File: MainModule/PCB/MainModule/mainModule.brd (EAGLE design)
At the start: 160 x 100 mm, 13 parts, among them U1 LM5007MM

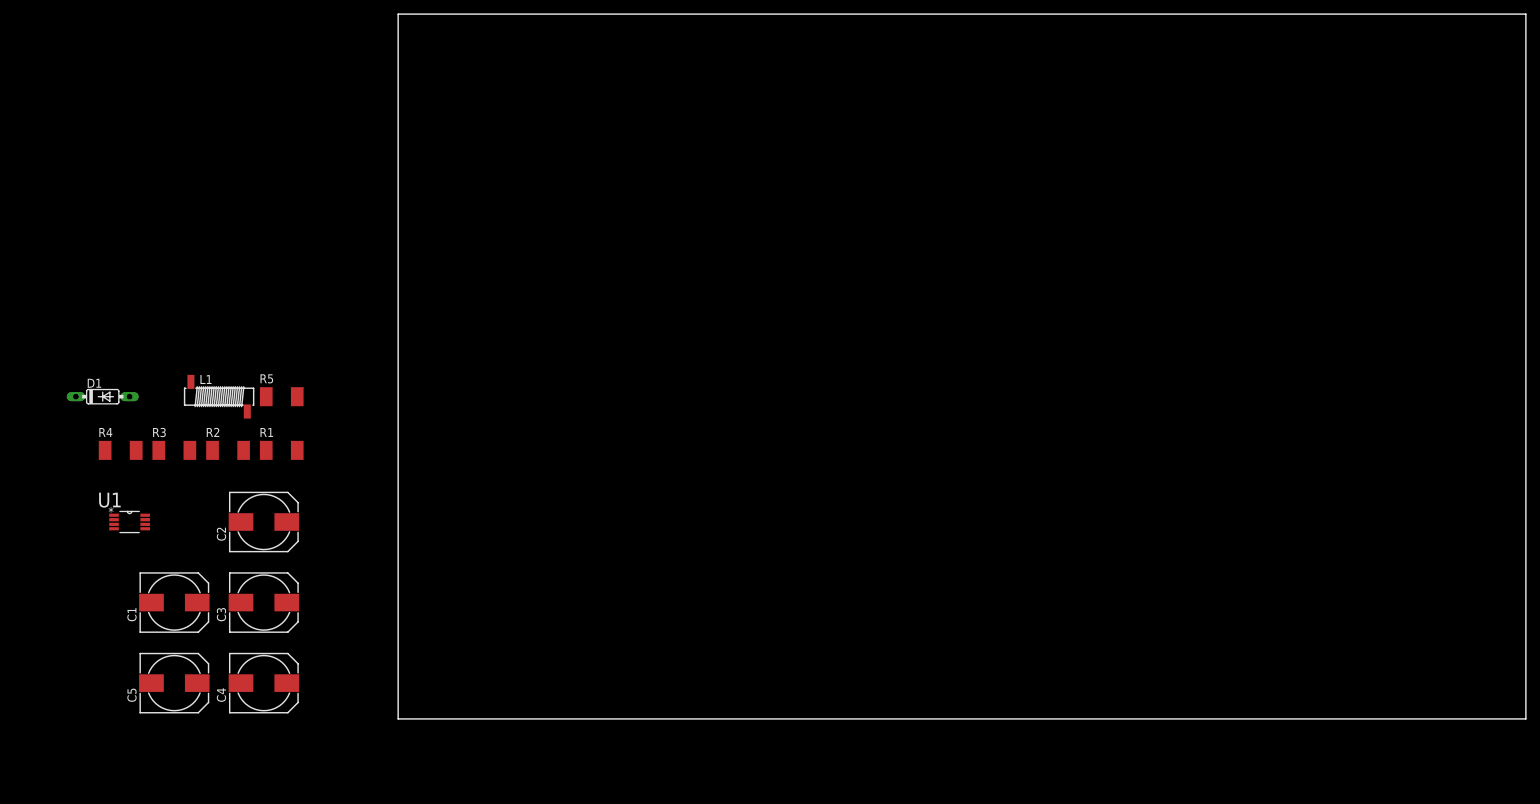
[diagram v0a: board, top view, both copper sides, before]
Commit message: Changed capacitor packages in to power supply schematic (switching)
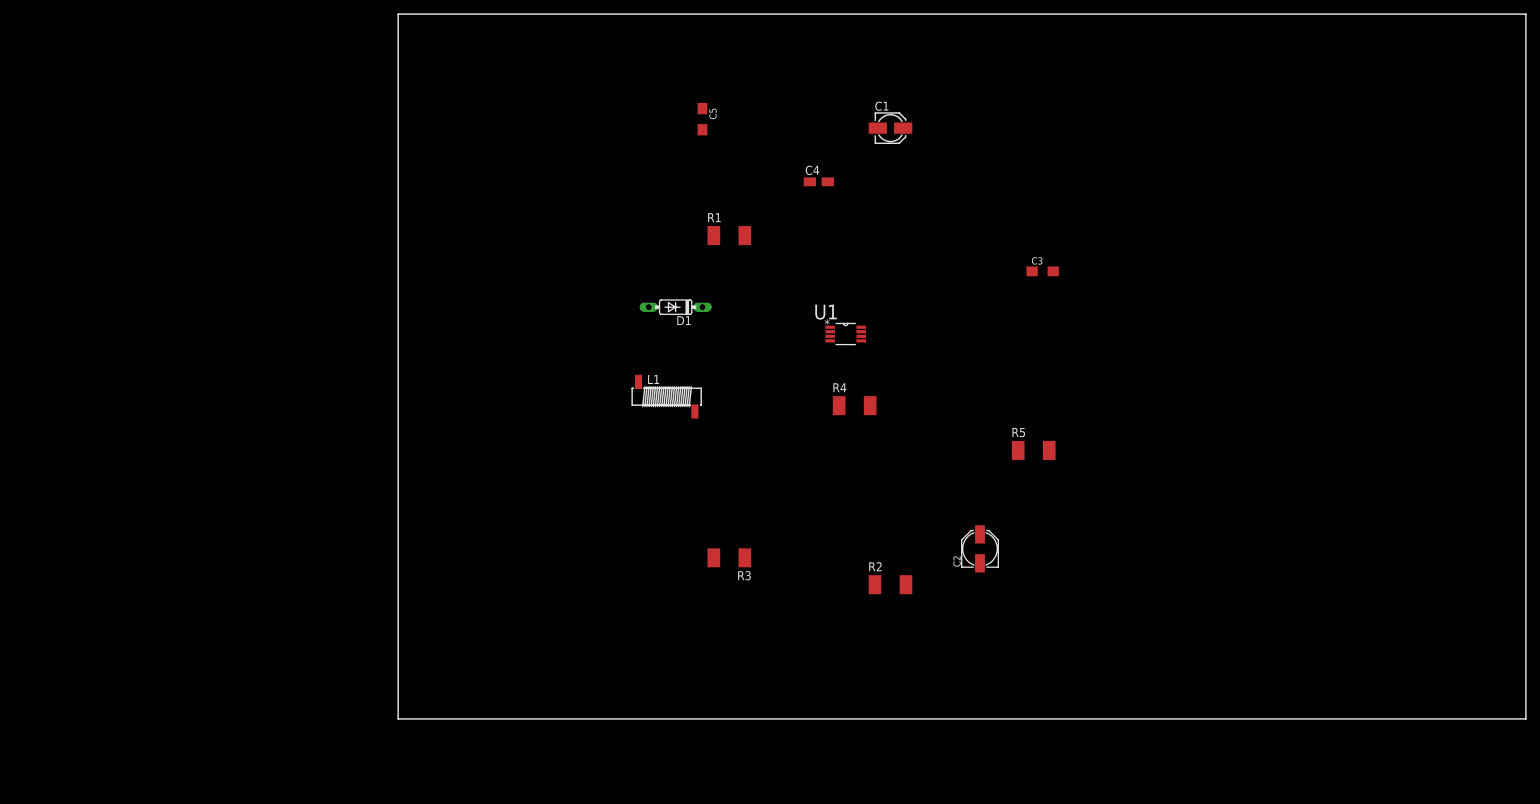
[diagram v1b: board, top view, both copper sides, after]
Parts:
- C1: device resistor:140CLH-0810 -> resistor:153CLV-0405
- C2: device resistor:140CLH-0810 -> resistor:PANASONIC_C
- C3: value 0.1uF, 50V -> 100nF, 50V; device resistor:140CLH-0810 -> resistor:SMC_A
- C4: value 0.01uF, 50V -> 10nF, 50V; device resistor:140CLH-0810 -> resistor:R/2012-12W
- C5: value 0.1uF, 100V -> 100nF, 100V; device resistor:140CLH-0810 -> resistor:SMC_A
- moved C1 121.9 mm to (69.8, 83.8)
- moved C3 120.1 mm to (91.4, 63.5)
- moved C5 109.6 mm to (43.2, 85.1), turned to 270 degrees
- moved R5 107.0 mm to (90.2, 38.1)
- moved C4 106.1 mm to (59.7, 76.2)
- moved U1 105.0 mm to (63.5, 54.6)
- moved R4 104.3 mm to (64.8, 44.5)
- moved C2 101.7 mm to (82.5, 24.1), turned to 90 degrees
- moved R2 95.9 mm to (69.8, 19.1)
- moved D1 82.3 mm to (39.4, 58.4), turned to 180 degrees
- moved R3 80.2 mm to (47.0, 22.9), turned to 180 degrees
- moved R1 70.4 mm to (47.0, 68.6)
- moved L1 63.5 mm to (38.1, 45.7)
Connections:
- net GND: no longer C1.-, C2.-, C3.-, C5.-
- net N$5: no longer C4.+
- net N$6: no longer C4.-
- net N$7: no longer C3.+
- net N$9: no longer C2.+
- net VIN(12-75V): no longer C1.+, C5.+
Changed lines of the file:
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@@
 </autorouter>
 <elements>
-<element name="U1" library="LM5007" package="SOP65P490X109-8N" value="LM5007MM" x="-38.1" y="27.94">
-<attribute name="PACKAGE" value="SOP-8" x="0" y="0" size="1.778" layer="27" display="off"/>
-<attribute name="OC_NEWARK" value="97K3542" x="0" y="0" size="1.778" layer="27" display="off"/>
-<attribute name="MPN" value="LM5007MM" x="0" y="0" size="1.778" layer="27" display="off"/>
-<attribute name="SUPPLIER" value="TEXAS INSTRUMENTS" x="0" y="0" size="1.778" layer="27" display="off"/>
-<attribute name="OC_FARNELL" value="9779345" x="0" y="0" size="1.778" layer="27" display="off"/>
+<element name="U1" library="LM5007" package="SOP65P490X109-8N" value="LM5007MM" x="63.5" y="54.61">
+<attribute name="PACKAGE" value="SOP-8" x="101.6" y="26.67" size="1.778" layer="27" display="off"/>
+<attribute name="OC_NEWARK" value="97K3542" x="101.6" y="26.67" size="1.778" layer="27" display="off"/>
+<attribute name="MPN" value="LM5007MM" x="101.6" y="26.67" size="1.778" layer="27" display="off"/>
+<attribute name="SUPPLIER" value="TEXAS INSTRUMENTS" x="101.6" y="26.67" size="1.778" layer="27" display="off"/>
+<attribute name="OC_FARNELL" value="9779345" x="101.6" y="26.67" size="1.778" layer="27" display="off"/>
 </element>
-<element name="C1" library="resistor" package="140CLH-0810" value="1uF, 100V" x="-31.75" y="16.51"/>
-<element name="C2" library="resistor" package="140CLH-0810" value="15uF, 25V" x="-19.05" y="27.94"/>
-<element name="C3" library="resistor" package="140CLH-0810" value="0.1uF, 50V" x="-19.05" y="16.51"/>
-<element name="C4" library="resistor" package="140CLH-0810" value="0.01uF, 50V" x="-19.05" y="5.08"/>
-<element name="C5" library="resistor" package="140CLH-0810" value="0.1uF, 100V" x="-31.75" y="5.08"/>
-<element name="L1" library="inductor-neosid" package="SM-Z15" value="100uH" x="-25.4" y="45.72">
-<attribute name="OC_NEWARK" value="unknown" x="0" y="0" size="1.778" layer="27" display="off"/>
-<attribute name="MPN" value="" x="0" y="0" size="1.778" layer="27" display="off"/>
-<attribute name="MF" value="" x="0" y="0" size="1.778" layer="27" display="off"/>
-<attribute name="OC_FARNELL" value="unknown" x="0" y="0" size="1.778" layer="27" display="off"/>
+<element name="C1" library="resistor" package="153CLV-0405" value="1uF, 100V" x="69.85" y="83.82"/>
+<element name="C2" library="resistor" package="PANASONIC_C" value="15uF, 25V" x="82.55" y="24.13" rot="R90"/>
+<element name="C3" library="resistor" package="SMC_A" value="100nF, 50V" x="91.44" y="63.5"/>
+<element name="C4" library="resistor" package="R/2012-12W" value="10nF, 50V" x="59.69" y="76.2"/>
+<element name="C5" library="resistor" package="SMC_A" value="100nF, 100V" x="43.18" y="85.09" rot="R270"/>
+<element name="L1" library="inductor-neosid" package="SM-Z15" value="100uH" x="38.1" y="45.72">
+<attribute name="OC_NEWARK" value="unknown" x="63.5" y="0" size="1.778" layer="27" display="off"/>
+<attribute name="MPN" value="" x="63.5" y="0" size="1.778" layer="27" display="off"/>
+<attribute name="MF" value="" x="63.5" y="0" size="1.778" layer="27" display="off"/>
+<attribute name="OC_FARNELL" value="unknown" x="63.5" y="0" size="1.778" layer="27" display="off"/>
 </element>
-<element name="R1" library="rcl" package="R2010" value="200K" x="-16.51" y="38.1"/>
-<element name="R2" library="rcl" package="R2010" value="100K" x="-24.13" y="38.1"/>
-<element name="R3" library="rcl" package="R2010" value="1K" x="-31.75" y="38.1"/>
-<element name="R4" library="rcl" package="R2010" value="1K" x="-39.37" y="38.1"/>
-<element name="R5" library="rcl" package="R2010" value="1ohm" x="-16.51" y="45.72"/>
-<element name="D1" library="diode" package="DO35-7" value="1N4148DO35-7" x="-41.91" y="45.72"/>
+<element name="R1" library="rcl" package="R2010" value="200K" x="46.99" y="68.58"/>
+<element name="R2" library="rcl" package="R2010" value="100K" x="69.85" y="19.05"/>
+<element name="R3" library="rcl" package="R2010" value="1K" x="46.99" y="22.86" rot="R180"/>
+<element name="R4" library="rcl" package="R2010" value="1K" x="64.77" y="44.45"/>
+<element name="R5" library="rcl" package="R2010" value="1ohm" x="90.17" y="38.1"/>
+<element name="D1" library="diode" package="DO35-7" value="1N4148DO35-7" x="39.37" y="58.42" rot="R180"/>
 </elements>
 <signals>
@@
 <contactref element="U1" pad="3"/>
 <contactref element="R2" pad="2"/>
-<wire x1="-40.3098" y1="27.6098" x2="-21.93" y2="38.1" width="0" layer="19" extent="1-1"/>
+<wire x1="61.2902" y1="54.2798" x2="72.05" y2="19.05" width="0" layer="19" extent="1-1"/>
 </signal>
 <signal name="N$3">
 <contactref element="U1" pad="6"/>
 <contactref element="R1" pad="1"/>
-<wire x1="-35.8902" y1="27.6098" x2="-18.71" y2="38.1" width="0" layer="19" extent="1-1"/>
+<wire x1="65.7098" y1="54.2798" x2="44.79" y2="68.58" width="0" layer="19" extent="1-1"/>
 </signal>
 <signal name="VIN(12-75V)">
 <contactref element="U1" pad="8"/>
 <contactref element="R1" pad="2"/>
-<contactref element="C1" pad="+"/>
-<contactref element="C5" pad="+"/>
-<wire x1="-35.8902" y1="28.9052" x2="-14.31" y2="38.1" width="0" layer="19" extent="1-1"/>
-<wire x1="-28.5" y1="16.51" x2="-35.8902" y2="28.9052" width="0" layer="19" extent="1-1"/>
-<wire x1="-28.5" y1="5.08" x2="-28.5" y2="16.51" width="0" layer="19" extent="1-1"/>
+<wire x1="65.7098" y1="55.5752" x2="49.19" y2="68.58" width="0" layer="19" extent="1-1"/>
+<wire x1="73.1" y1="83.82" x2="65.7098" y2="55.5752" width="0" layer="19" extent="1-1"/>
+<wire x1="43.18" y1="81.84" x2="73.1" y2="83.82" width="0" layer="19" extent="1-1"/>
 </signal>
 <signal name="N$5">
-<contactref element="C4" pad="+"/>
 <contactref element="U1" pad="2"/>
-<wire x1="-40.3098" y1="28.2702" x2="-15.8" y2="5.08" width="0" layer="19" extent="1-1"/>
+<wire x1="61.2902" y1="54.9402" x2="62.94" y2="76.2" width="0" layer="19" extent="1-1"/>
 </signal>
 <signal name="N$6">
-<contactref element="C4" pad="-"/>
 <contactref element="U1" pad="1"/>
 <contactref element="D1" pad="C"/>
 <contactref element="L1" pad="1"/>
-<wire x1="-45.72" y1="45.72" x2="-29.4" y2="47.82" width="0" layer="19" extent="1-1"/>
-<wire x1="-40.3098" y1="28.9052" x2="-45.72" y2="45.72" width="0" layer="19" extent="1-1"/>
-<wire x1="-22.3" y1="5.08" x2="-40.3098" y2="28.9052" width="0" layer="19" extent="1-1"/>
+<wire x1="43.18" y1="58.42" x2="34.1" y2="47.82" width="0" layer="19" extent="1-1"/>
+<wire x1="61.2902" y1="55.5752" x2="43.18" y2="58.42" width="0" layer="19" extent="1-1"/>
+<wire x1="56.44" y1="76.2" x2="61.2902" y2="55.5752" width="0" layer="19" extent="1-1"/>
 </signal>
 <signal name="GND">
-<contactref element="C3" pad="-"/>
-<contactref element="C1" pad="-"/>
-<contactref element="C5" pad="-"/>
 <contactref element="R2" pad="1"/>
 <contactref element="U1" pad="4"/>
 <contactref element="R4" pad="1"/>
-<contactref element="C2" pad="-"/>
 <contactref element="D1" pad="A"/>
-<wire x1="-35" y1="16.51" x2="-35" y2="5.08" width="0" layer="19" extent="1-1"/>
-<wire x1="-40.3098" y1="26.9748" x2="-35" y2="16.51" width="0" layer="19" extent="1-1"/>
-<wire x1="-41.57" y1="38.1" x2="-40.3098" y2="26.9748" width="0" layer="19" extent="1-1"/>
-<wire x1="-38.1" y1="45.72" x2="-41.57" y2="38.1" width="0" layer="19" extent="1-1"/>
-<wire x1="-22.3" y1="16.51" x2="-35" y2="16.51" width="0" layer="19" extent="1-1"/>
-<wire x1="-22.3" y1="27.94" x2="-22.3" y2="16.51" width="0" layer="19" extent="1-1"/>
-<wire x1="-26.33" y1="38.1" x2="-22.3" y2="27.94" width="0" layer="19" extent="1-1"/>
+<wire x1="66.6" y1="83.82" x2="43.18" y2="88.34" width="0" layer="19" extent="1-1"/>
+<wire x1="61.2902" y1="53.6448" x2="66.6" y2="83.82" width="0" layer="19" extent="1-1"/>
+<wire x1="62.57" y1="44.45" x2="61.2902" y2="53.6448" width="0" layer="19" extent="1-1"/>
+<wire x1="35.56" y1="58.42" x2="62.57" y2="44.45" width="0" layer="19" extent="1-1"/>
+<wire x1="88.19" y1="63.5" x2="66.6" y2="83.82" width="0" layer="19" extent="1-1"/>
+<wire x1="82.55" y1="20.88" x2="88.19" y2="63.5" width="0" layer="19" extent="1-1"/>
+<wire x1="67.65" y1="19.05" x2="82.55" y2="20.88" width="0" layer="19" extent="1-1"/>
 </signal>
 <signal name="N$7">
 <contactref element="U1" pad="7"/>
-<contactref element="C3" pad="+"/>
-<wire x1="-15.8" y1="16.51" x2="-35.8902" y2="28.2702" width="0" layer="19" extent="1-1"/>
+<wire x1="94.69" y1="63.5" x2="65.7098" y2="54.9402" width="0" layer="19" extent="1-1"/>
 </signal>
 <signal name="VOUT(5V)">
@@
 <contactref element="R5" pad="2"/>
 <contactref element="R3" pad="2"/>
-<wire x1="-21.4" y1="43.62" x2="-14.31" y2="45.72" width="0" layer="19" extent="1-1"/>
-<wire x1="-29.55" y1="38.1" x2="-21.4" y2="43.62" width="0" layer="19" extent="1-1"/>
+<wire x1="42.1" y1="43.62" x2="92.37" y2="38.1" width="0" layer="19" extent="1-1"/>
+<wire x1="44.79" y1="22.86" x2="42.1" y2="43.62" width="0" layer="19" extent="1-1"/>
 </signal>
 <signal name="N$8">
@@
 <contactref element="R4" pad="2"/>
 <contactref element="U1" pad="5"/>
-<wire x1="-37.17" y1="38.1" x2="-35.8902" y2="26.9748" width="0" layer="19" extent="1-1"/>
-<wire x1="-33.95" y1="38.1" x2="-37.17" y2="38.1" width="0" layer="19" extent="1-1"/>
+<wire x1="66.97" y1="44.45" x2="65.7098" y2="53.6448" width="0" layer="19" extent="1-1"/>
+<wire x1="49.19" y1="22.86" x2="66.97" y2="44.45" width="0" layer="19" extent="1-1"/>
 </signal>
 <signal name="N$9">
 <contactref element="R5" pad="1"/>
-<contactref element="C2" pad="+"/>
-<wire x1="-15.8" y1="27.94" x2="-18.71" y2="45.72" width="0" layer="19" extent="1-1"/>
+<wire x1="82.55" y1="27.38" x2="87.97" y2="38.1" width="0" layer="19" extent="1-1"/>
 </signal>
 </signals>

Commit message: Added linear regulator LM3940.lbr library
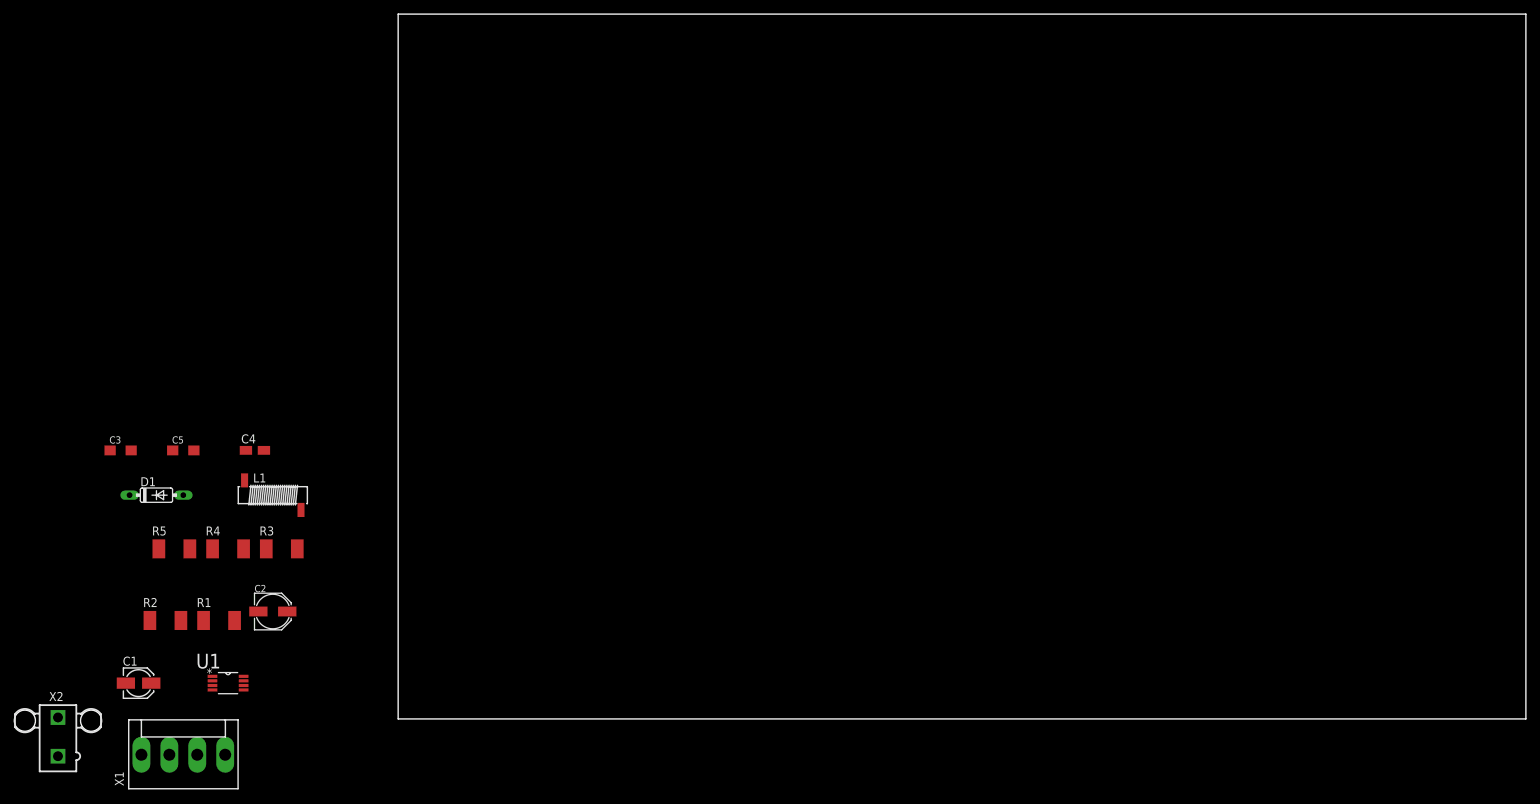
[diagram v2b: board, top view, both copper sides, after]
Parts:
- added X1: (no value), con-molex:KK-156-4
- added X2: 5566-2, con-molex:5566-2
- moved C3 133.3 mm to (-39.4, 38.1)
- moved C1 132.6 mm to (-36.8, 5.08)
- moved R5 122.7 mm to (-31.8, 24.1)
- moved R2 103.0 mm to (-33.0, 14.0)
- moved C2 100.7 mm to (-17.8, 15.2), turned to 0 degrees
- moved U1 100.7 mm to (-24.1, 5.08)
- moved R4 91.2 mm to (-24.1, 24.1)
- moved R1 90.7 mm to (-25.4, 14.0)
- moved C4 88.6 mm to (-20.3, 38.1)
- moved C5 87.4 mm to (-30.5, 38.1), turned to 0 degrees
- moved D1 78.3 mm to (-34.3, 31.8), turned to 0 degrees
- moved R3 63.5 mm to (-16.5, 24.1), turned to 0 degrees
- moved L1 57.6 mm to (-17.8, 31.8)
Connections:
- net GND: now also C1.-, C2.-, C3.-, C5.-, X2.1
- net N$5: now also C4.+
- net N$6: now also C4.-
- net N$7: now also C3.+
- net N$9: now also C2.+
- net VIN(12-75V): now also C1.+, C5.+, X2.2
